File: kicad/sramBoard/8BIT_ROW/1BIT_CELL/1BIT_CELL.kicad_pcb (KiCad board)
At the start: 4 copper layers, 8 parts, among them Q1 NMOS, Q2 NMOS, Q3 PMOS, Q4 NMOS, Q5 PMOS, Q6 NMOS, Q7 NMOS, Q8 NMOS

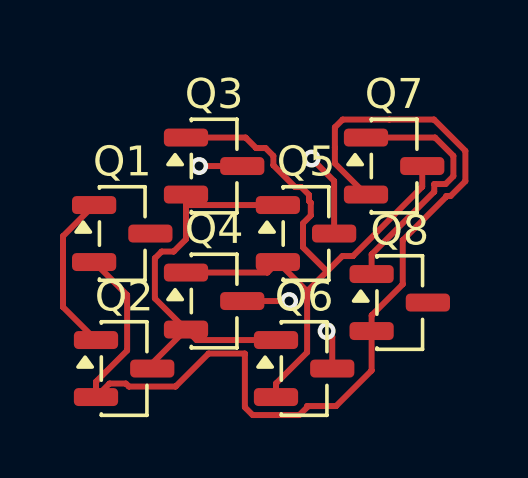
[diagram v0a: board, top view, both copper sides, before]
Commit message: add pmos resistors
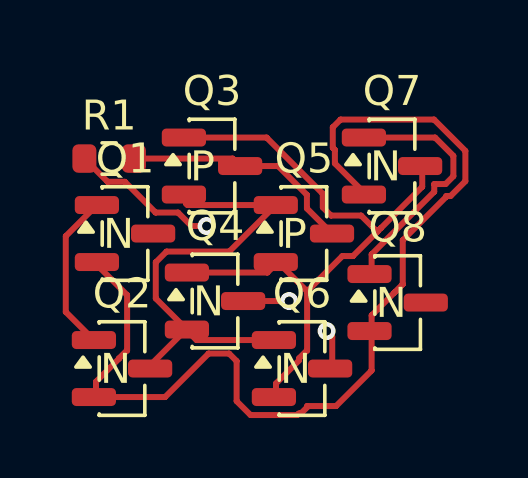
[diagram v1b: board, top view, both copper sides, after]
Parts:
- added R1: 47R, Resistor_SMD:R_0603_1608Metric, F.Cu at (122.5, 77.8)
- Q1, Q2, Q4, Q6, Q7, Q8: footprint Package_TO_SOT_SMD:SOT-23 -> easyeda2kicad:SOT-23-N
- Q3, Q5: footprint Package_TO_SOT_SMD:SOT-23 -> easyeda2kicad:SOT-23-P
- moved Q1 0.16 mm to (123.1, 80.2)
- moved Q4 0.10 mm to (126.1, 82.5)
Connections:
- net +5V renamed Net-(Q3-S)
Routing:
- net +5V: track 0.00 -> 5.01 mm, vias 0 -> 1
- net Net-(Q3-S): track 4.25 -> 7.91 mm, vias 2 -> 0
- net Net-(Q2-S): track 13.6 -> 15.8 mm

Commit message: finish main pcb
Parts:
- added D1: LED, LED_SMD:LED_0805_2012Metric_Pad1.15x1.40mm_HandSolder, B.Cu at (129.2, 81.0)
- added Q9: NMOS, easyeda2kicad:SOT-23-N, B.Cu at (127.0, 78.0)
- added R2: 220R, Resistor_SMD:R_0603_1608Metric_Pad0.98x0.95mm_HandSolder, B.Cu at (129.8, 78.2)
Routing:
- net Net-(Q2-S): track 15.8 -> 19.4 mm, vias 0 -> 1
- net Net-(D1-A): track 0.00 -> 2.47 mm
- net GND: track 2.89 -> 5.29 mm
- net Net-(Q9-S): track 0.00 -> 2.16 mm
- net +5V: track 5.01 -> 6.36 mm

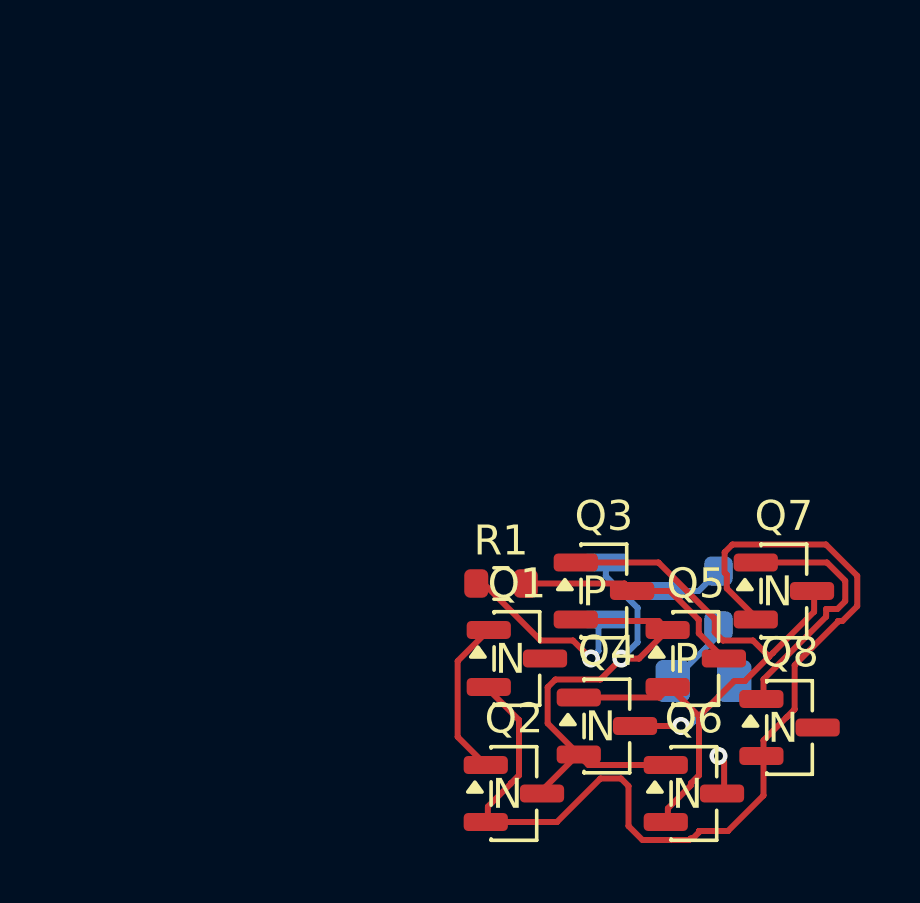
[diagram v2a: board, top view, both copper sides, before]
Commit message: fix main ram board
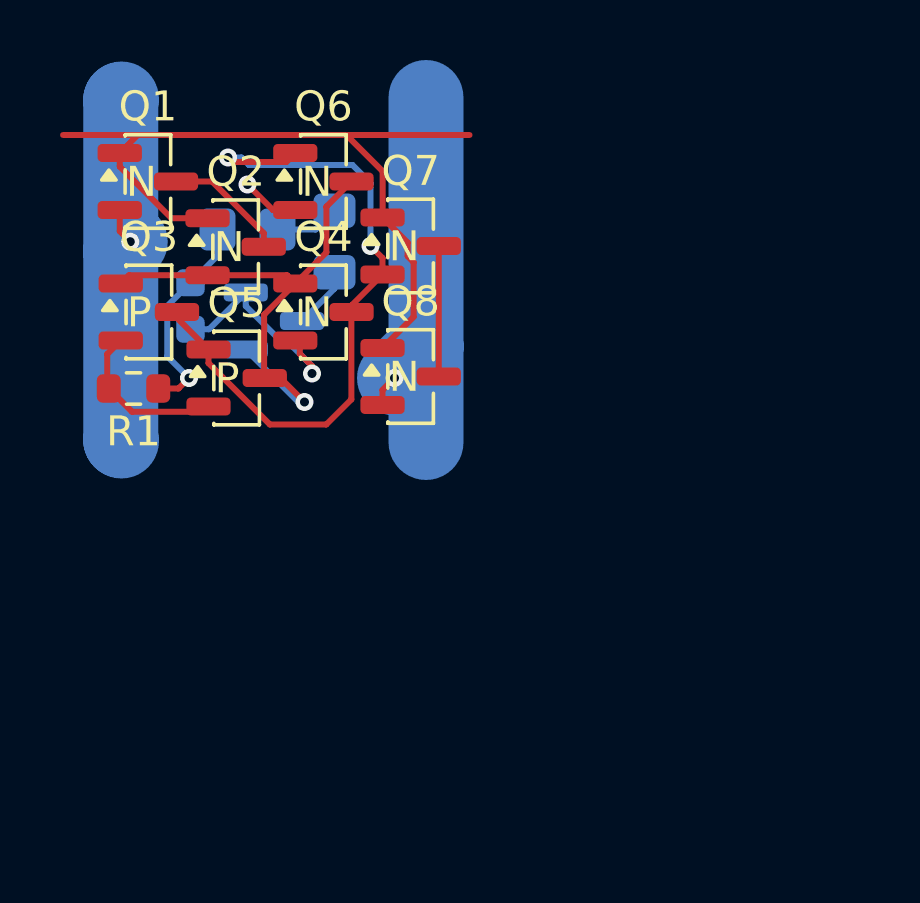
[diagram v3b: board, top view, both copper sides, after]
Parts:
- added C1: 100nC, Capacitor_SMD:C_0603_1608Metric, B.Cu at (112.2, 68.5)
- Q1, Q2, Q4, Q6, Q7, Q8, Q9: value NMOS -> Q_NMOS_GSD
- Q3, Q5: value PMOS -> Q_PMOS_GSD
- R2: value 220R -> 470R; footprint Resistor_SMD:R_0603_1608Metric_Pad0.98x0.95mm_HandSolder -> Resistor_SMD:R_0805_2012Metric_Pad1.20x1.40mm_HandSolder
- moved Q6 23.8 mm to (116.7, 64.3)
- moved Q2 20.4 mm to (113.7, 66.5)
- moved Q1 20.1 mm to (110.8, 64.3)
- moved R2 19.9 mm to (114.0, 66.0), turned to 0 degrees
- moved D1 19.1 mm to (117.0, 66.3), turned to 90 degrees
- moved Q5 17.9 mm to (113.8, 70.9)
- moved Q3 17.8 mm to (110.8, 68.7)
- moved Q8 17.2 mm to (119.6, 70.8)
- moved Q7 16.9 mm to (119.6, 66.5)
- moved Q4 16.7 mm to (116.7, 68.7)
- moved Q9 15.0 mm to (115.0, 69.0)
- moved R1 13.9 mm to (110.2, 71.2), turned to 180 degrees
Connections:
- D1 pad 1: GND -> Net-(D1-K)
- Q1 pad 1: Net-(Q1-D) -> /WL
- Q1 pad 2: /WL -> /BL
- Q1 pad 3: /BL -> Net-(Q1-D)
- Q2 pad 1: Net-(Q1-D) -> /WL
- Q2 pad 2: /WL -> Net-(Q2-S)
- Q2 pad 3: Net-(Q2-S) -> Net-(Q1-D)
- Q3 pad 1: Net-(Q3-D) -> Net-(Q2-S)
- Q3 pad 2: Net-(Q2-S) -> Net-(Q3-S)
- Q3 pad 3: Net-(Q3-S) -> Net-(Q3-D)
- Q4 pad 1: Net-(Q3-D) -> Net-(Q2-S)
- Q4 pad 2: Net-(Q2-S) -> GND
- Q4 pad 3: GND -> Net-(Q3-D)
- Q5 pad 1: Net-(Q2-S) -> Net-(Q3-D)
- Q5 pad 2: Net-(Q3-D) -> Net-(Q3-S)
- Q5 pad 3: Net-(Q3-S) -> Net-(Q2-S)
- Q6 pad 1: Net-(Q2-S) -> Net-(Q3-D)
- Q6 pad 2: Net-(Q3-D) -> GND
- Q6 pad 3: GND -> Net-(Q2-S)
- Q7 pad 1: Net-(Q7-D) -> /WL
- Q7 pad 2: /WL -> Net-(Q3-D)
- Q7 pad 3: Net-(Q3-D) -> Net-(Q7-D)
- Q8 pad 1: Net-(Q7-D) -> /WL
- Q8 pad 2: /WL -> /~{BL_{1}}
- Q8 pad 3: /~{BL_{1}} -> Net-(Q7-D)
- Q9 pad 1: +5V -> Net-(Q2-S)
- Q9 pad 2: Net-(Q2-S) -> GND
- Q9 pad 3: Net-(Q9-S) -> Net-(D1-K)
- R2 pad 1: Net-(Q9-S) -> +5V
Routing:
- net /~{BL_{1}}: track 0.00 -> 14.1 mm, vias 0 -> 1
- net /BL: track 0.00 -> 13.1 mm, vias 0 -> 1
- net /WL: track 33.9 -> 27.0 mm
- net GND: track 5.29 -> 9.44 mm
- net Net-(Q7-D): track 8.46 -> 4.35 mm
- net Net-(Q3-S): track 7.91 -> 5.50 mm
- net Net-(Q9-S): track 2.16 -> 0.00 mm
- net Net-(D1-K): track 0.00 -> 2.07 mm
- net Net-(Q2-S): track 19.4 -> 18.2 mm
- net Net-(Q1-D): track 5.32 -> 4.09 mm
- net +5V: track 6.36 -> 7.36 mm
- net Net-(Q3-D): track 22.5 -> 23.4 mm, vias 0 -> 2

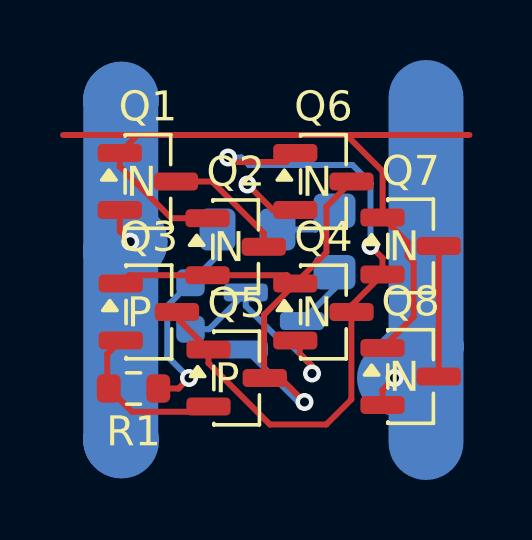
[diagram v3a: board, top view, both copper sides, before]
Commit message: Add breakout board through holes on main ram board
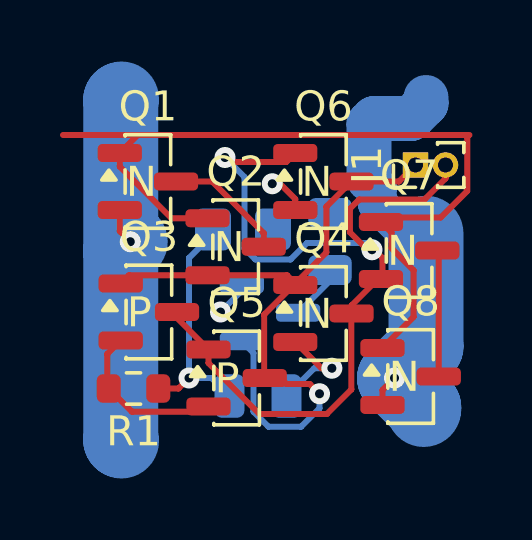
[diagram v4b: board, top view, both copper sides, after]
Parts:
- added J1: Conn_01x02_Pin, Connector_PinHeader_1.00mm:PinHeader_1x02_P1.00mm_Vertical, F.Cu at (119.7, 63.8)
- C1: footprint Capacitor_SMD:C_0603_1608Metric -> Capacitor_SMD:C_0805_2012Metric
- D1: footprint LED_SMD:LED_0805_2012Metric_Pad1.15x1.40mm_HandSolder -> Capacitor_SMD:C_0805_2012Metric
- R2: value 470R -> 360R
- moved C1 3.75 mm to (114.4, 71.5), turned to 0 degrees
- moved Q9 0.30 mm to (114.9, 68.7)
- moved Q7 0.16 mm to (119.5, 66.7)
- moved D1 0.15 mm to (116.8, 66.3)
- moved R2 0.15 mm to (113.9, 66.0)
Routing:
- net Net-(J1-Pin_2): track 23.4 -> 29.8 mm
- net Net-(J1-Pin_1): track 18.2 -> 23.9 mm
- net GND: track 9.44 -> 6.26 mm, vias 2 -> 3
- net /WL: track 27.0 -> 28.7 mm
- net +5V: track 7.36 -> 8.30 mm
- net /~{BL_{1}}: track 14.1 -> 15.0 mm
